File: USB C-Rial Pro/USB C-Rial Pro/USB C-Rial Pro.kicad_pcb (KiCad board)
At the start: 2 copper layers, 44.5 x 16.3 mm, 32 parts, among them J1 USB_C_Receptacle_USB2.0, J2 Conn_01x06, SW1 SW_SPDT, U1 SPX3819M5-L-3-3, U2 CY7C65213-28PVXI

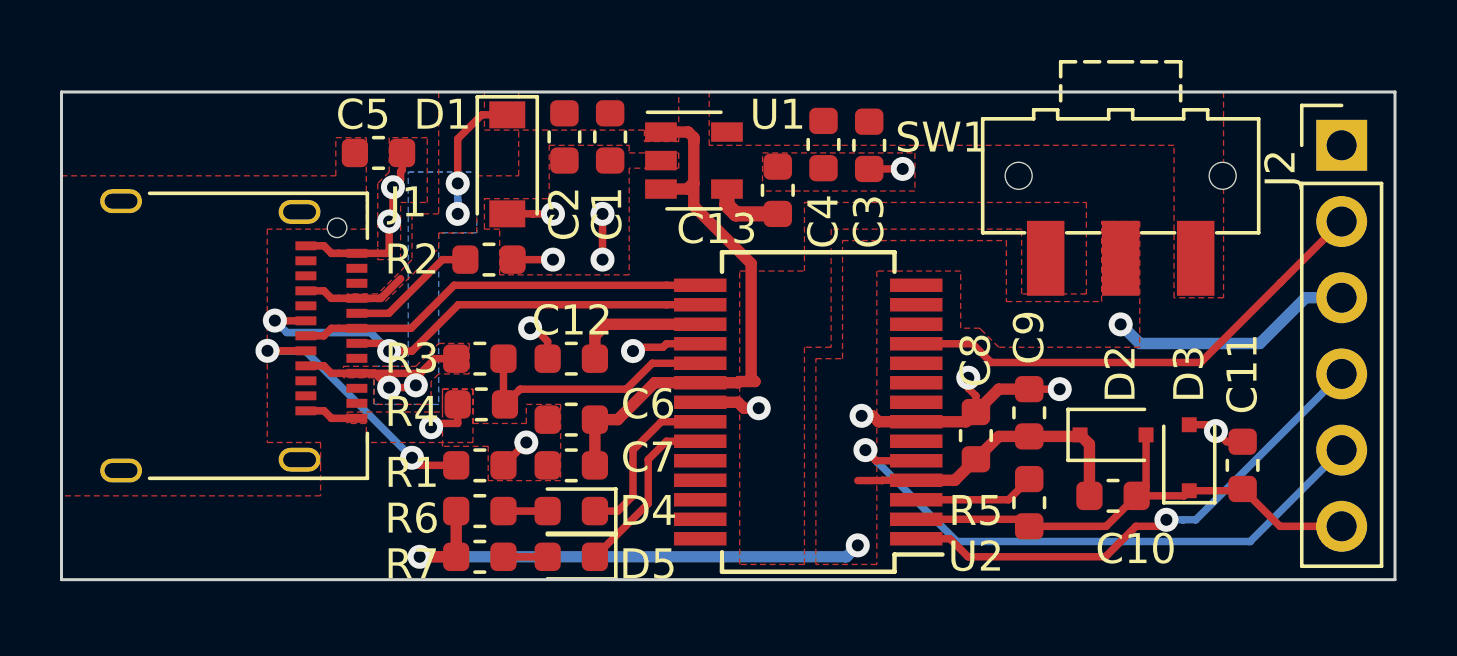
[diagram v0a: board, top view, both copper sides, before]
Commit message: Update Repository Info
Added Readme, render, BOM
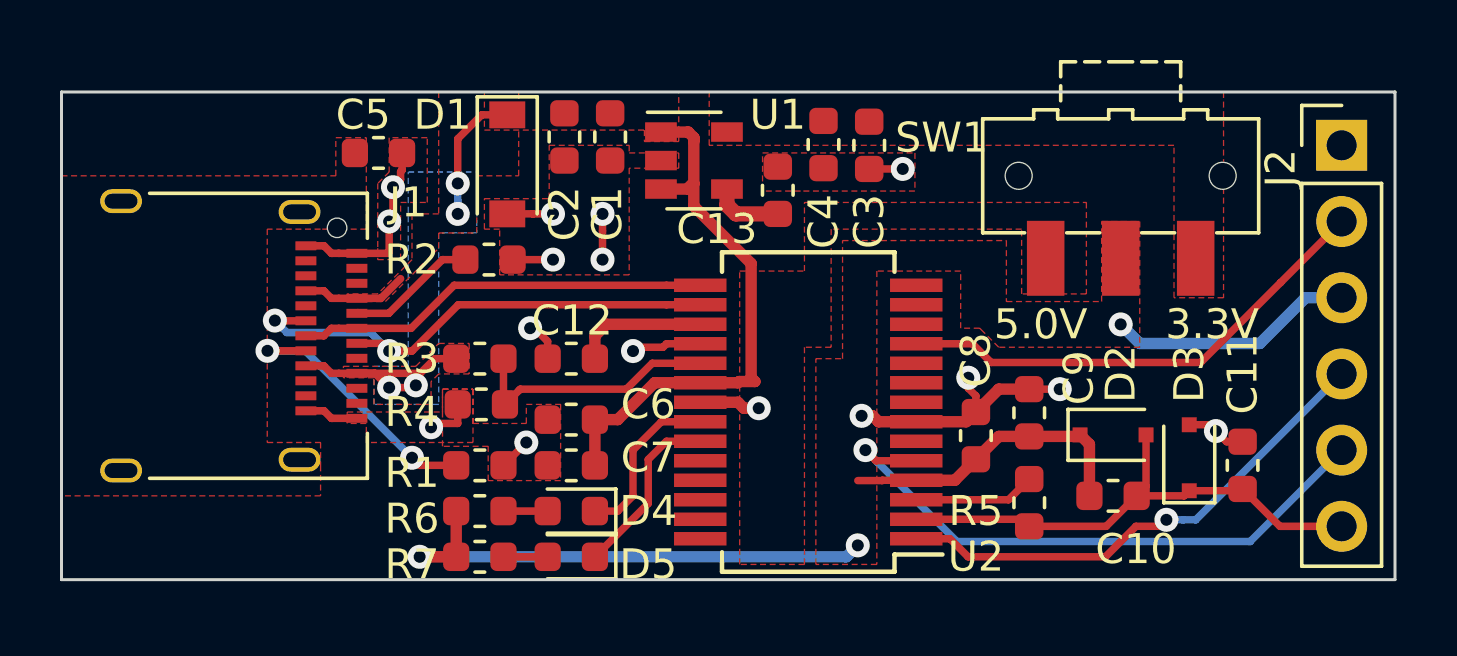
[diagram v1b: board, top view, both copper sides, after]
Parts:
- added G***: LOGO, logo:logo, B.Cu at (101.3, 61.7)
- moved REF** 6.36 mm to (111.9, 68.2)
- moved REF** 5.60 mm to (101.6, 68.1)
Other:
- board text added: "3.3V"
- board text added: "5.0V"
